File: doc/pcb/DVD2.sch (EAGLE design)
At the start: 39 parts, among them IC1 TEENSY_3.1_BASIC_DVD_BP, IC2 74HC14N, IC3 7805, IC4 POLOLU_TB6612FNG

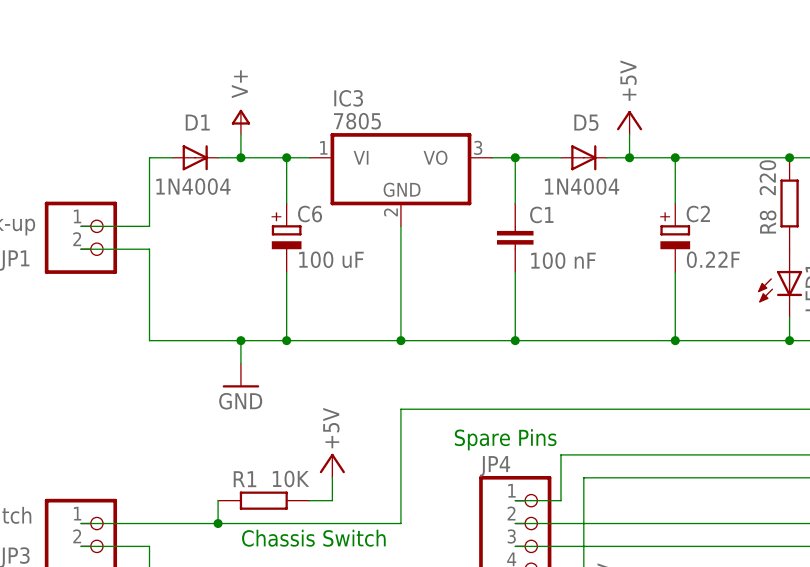
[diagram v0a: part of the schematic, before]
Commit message: Added additional diode to voltage regulator GND connection
Added diode to get the ref voltage correct
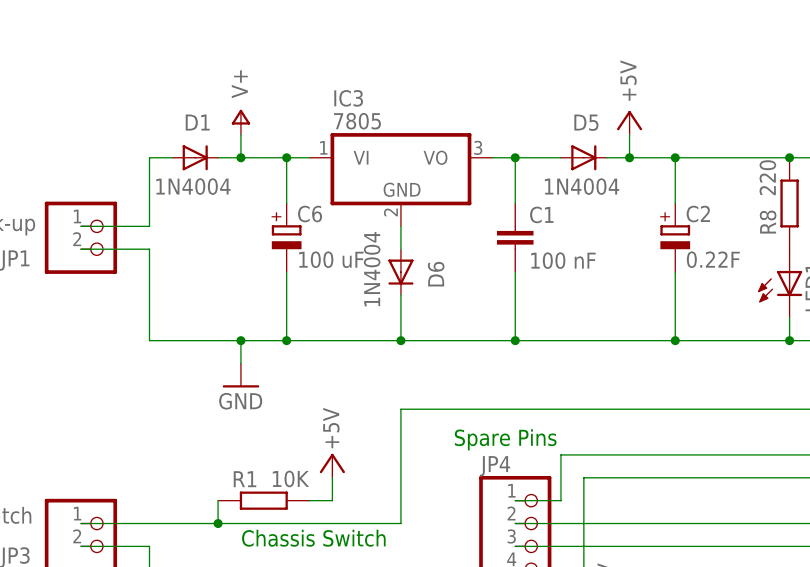
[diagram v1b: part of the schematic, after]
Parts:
- added D6: 1N4004, adafruit:1N4004
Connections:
- new net N$8: D6.A, IC3.GND
- net GND: now also D6.C; no longer IC3.GND
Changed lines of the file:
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@@
 <part name="GND16" library="supply1" deviceset="GND" device=""/>
 <part name="D5" library="adafruit" deviceset="1N4004" device=""/>
+<part name="D6" library="adafruit" deviceset="1N4004" device=""/>
 </parts>
 <sheets>
@@
 <attribute name="VALUE" x="46.228" y="150.8506" size="1.778" layer="96"/>
 </instance>
+<instance part="D6" gate="1" x="30.48" y="142.24" smashed="yes" rot="R270">
+<attribute name="NAME" x="33.5026" y="143.51" size="1.778" layer="95" rot="R270"/>
+<attribute name="VALUE" x="26.3906" y="146.812" size="1.778" layer="96" rot="R270"/>
+</instance>
 </instances>
 <busses>
@@
 <wire x1="12.7" y1="134.62" x2="17.78" y2="134.62" width="0.1524" layer="91"/>
 <wire x1="17.78" y1="134.62" x2="30.48" y2="134.62" width="0.1524" layer="91"/>
-<wire x1="30.48" y1="147.32" x2="30.48" y2="134.62" width="0.1524" layer="91"/>
+<junction x="12.7" y="134.62"/>
+<pinref part="LED1" gate="G$1" pin="C"/>
 <wire x1="30.48" y1="134.62" x2="43.18" y2="134.62" width="0.1524" layer="91"/>
-<junction x="12.7" y="134.62"/>
-<junction x="30.48" y="134.62"/>
-<pinref part="LED1" gate="G$1" pin="C"/>
 <wire x1="43.18" y1="134.62" x2="60.96" y2="134.62" width="0.1524" layer="91"/>
 <wire x1="60.96" y1="134.62" x2="73.66" y2="134.62" width="0.1524" layer="91"/>
@@
 <pinref part="JP1" gate="G$1" pin="2"/>
 <wire x1="2.54" y1="144.78" x2="-5.08" y2="144.78" width="0.1524" layer="91"/>
-<pinref part="IC3" gate="A1" pin="GND"/>
+<pinref part="D6" gate="1" pin="C"/>
+<wire x1="30.48" y1="139.7" x2="30.48" y2="134.62" width="0.1524" layer="91"/>
+<junction x="30.48" y="134.62"/>
 </segment>
 <segment>
@@
 </segment>
 </net>
+<net name="N$8" class="0">
+<segment>
+<pinref part="IC3" gate="A1" pin="GND"/>
+<pinref part="D6" gate="1" pin="A"/>
+<wire x1="30.48" y1="147.32" x2="30.48" y2="144.78" width="0.1524" layer="91"/>
+</segment>
+</net>

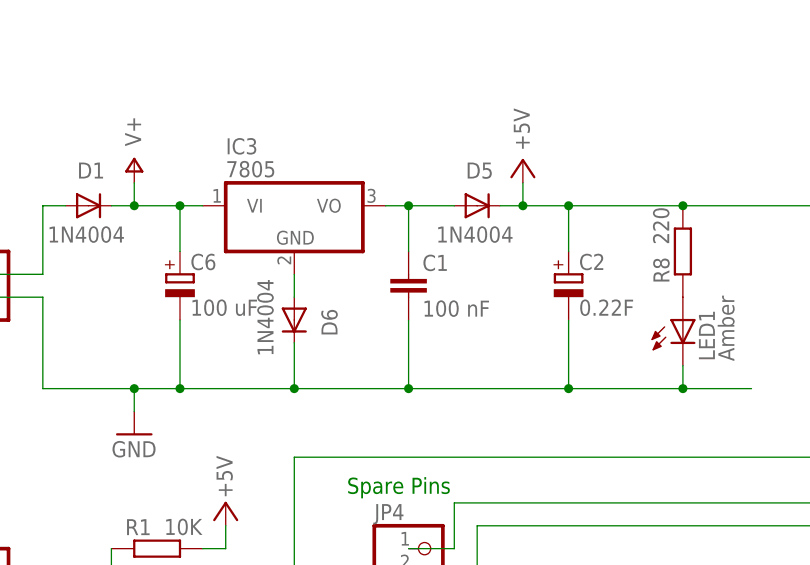
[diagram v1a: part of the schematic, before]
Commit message: Updated DVD2 with extra Diode(s)
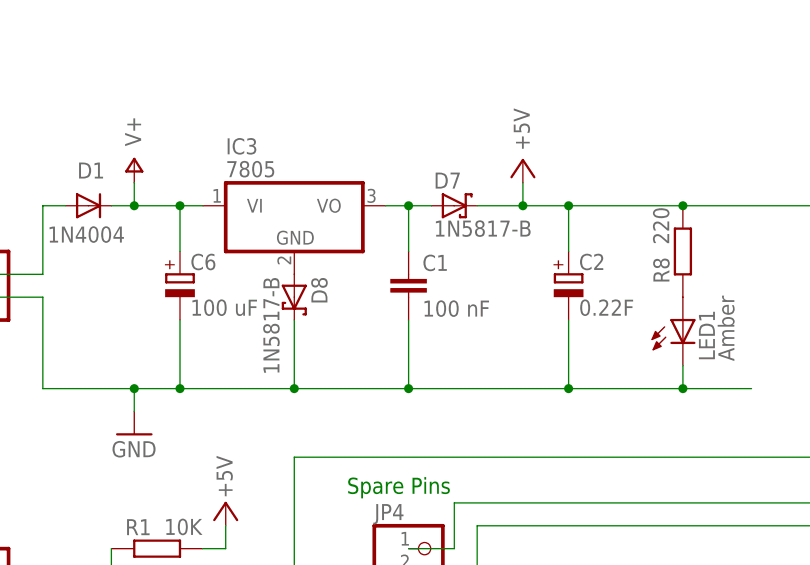
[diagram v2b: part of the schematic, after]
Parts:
- removed D5, D6: 1N4004, adafruit:1N4004
- added D7, D8: 1N5817-B, diode:1N5817-B
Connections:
- net +5V: now also D7.C; no longer D5.C
- net GND: now also D8.C; no longer D6.C
- net N$5: now also D7.A; no longer D5.A
- net N$8: now also D8.A; no longer D6.A
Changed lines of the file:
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@@
 <?xml version="1.0" encoding="utf-8"?>
 <!DOCTYPE eagle SYSTEM "eagle.dtd">
-<eagle version="7.3.0">
+<eagle version="7.5.0">
 <drawing>
 <settings>
@@
 <part name="P+12" library="supply1" deviceset="+5V" device=""/>
 <part name="GND16" library="supply1" deviceset="GND" device=""/>
-<part name="D5" library="adafruit" deviceset="1N4004" device=""/>
-<part name="D6" library="adafruit" deviceset="1N4004" device=""/>
+<part name="D7" library="diode" deviceset="1N581*" device="" technology="7-B"/>
+<part name="D8" library="diode" deviceset="1N581*" device="" technology="7-B"/>
 </parts>
 <sheets>
@@
 </instance>
 <instance part="GND16" gate="1" x="53.34" y="96.52"/>
-<instance part="D5" gate="1" x="50.8" y="154.94" smashed="yes">
-<attribute name="NAME" x="49.53" y="157.9626" size="1.778" layer="95"/>
-<attribute name="VALUE" x="46.228" y="150.8506" size="1.778" layer="96"/>
-</instance>
-<instance part="D6" gate="1" x="30.48" y="142.24" smashed="yes" rot="R270">
-<attribute name="NAME" x="33.5026" y="143.51" size="1.778" layer="95" rot="R270"/>
-<attribute name="VALUE" x="26.3906" y="146.812" size="1.778" layer="96" rot="R270"/>
-</instance>
+<instance part="D7" gate="G$1" x="48.26" y="154.94"/>
+<instance part="D8" gate="G$1" x="30.48" y="144.78" rot="R270"/>
 </instances>
 <busses>
@@
 <pinref part="JP1" gate="G$1" pin="2"/>
 <wire x1="2.54" y1="144.78" x2="-5.08" y2="144.78" width="0.1524" layer="91"/>
-<pinref part="D6" gate="1" pin="C"/>
-<wire x1="30.48" y1="139.7" x2="30.48" y2="134.62" width="0.1524" layer="91"/>
+<wire x1="30.48" y1="142.24" x2="30.48" y2="134.62" width="0.1524" layer="91"/>
 <junction x="30.48" y="134.62"/>
+<pinref part="D8" gate="G$1" pin="C"/>
 </segment>
 <segment>
@@
 <segment>
 <pinref part="P+2" gate="1" pin="+5V"/>
-<wire x1="53.34" y1="154.94" x2="55.88" y2="154.94" width="0.1524" layer="91"/>
+<wire x1="50.8" y1="154.94" x2="55.88" y2="154.94" width="0.1524" layer="91"/>
 <wire x1="55.88" y1="157.48" x2="55.88" y2="154.94" width="0.1524" layer="91"/>
 <wire x1="55.88" y1="154.94" x2="60.96" y2="154.94" width="0.1524" layer="91"/>
@@
 <wire x1="60.96" y1="149.86" x2="60.96" y2="154.94" width="0.1524" layer="91"/>
 <junction x="60.96" y="154.94"/>
-<pinref part="D5" gate="1" pin="C"/>
+<pinref part="D7" gate="G$1" pin="C"/>
 </segment>
 <segment>
@@
 <pinref part="C1" gate="G$1" pin="1"/>
 <wire x1="43.18" y1="154.94" x2="43.18" y2="149.86" width="0.1524" layer="91"/>
-<pinref part="D5" gate="1" pin="A"/>
-<wire x1="48.26" y1="154.94" x2="43.18" y2="154.94" width="0.1524" layer="91"/>
+<wire x1="45.72" y1="154.94" x2="43.18" y2="154.94" width="0.1524" layer="91"/>
 <junction x="43.18" y="154.94"/>
+<pinref part="D7" gate="G$1" pin="A"/>
 </segment>
 </net>
@@
 <segment>
 <pinref part="IC3" gate="A1" pin="GND"/>
-<pinref part="D6" gate="1" pin="A"/>
-<wire x1="30.48" y1="147.32" x2="30.48" y2="144.78" width="0.1524" layer="91"/>
-</segment>
-</net>
+<pinref part="D8" gate="G$1" pin="A"/>
+</segment>
+</net>
